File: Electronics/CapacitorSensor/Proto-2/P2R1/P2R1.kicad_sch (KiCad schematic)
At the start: 48 parts

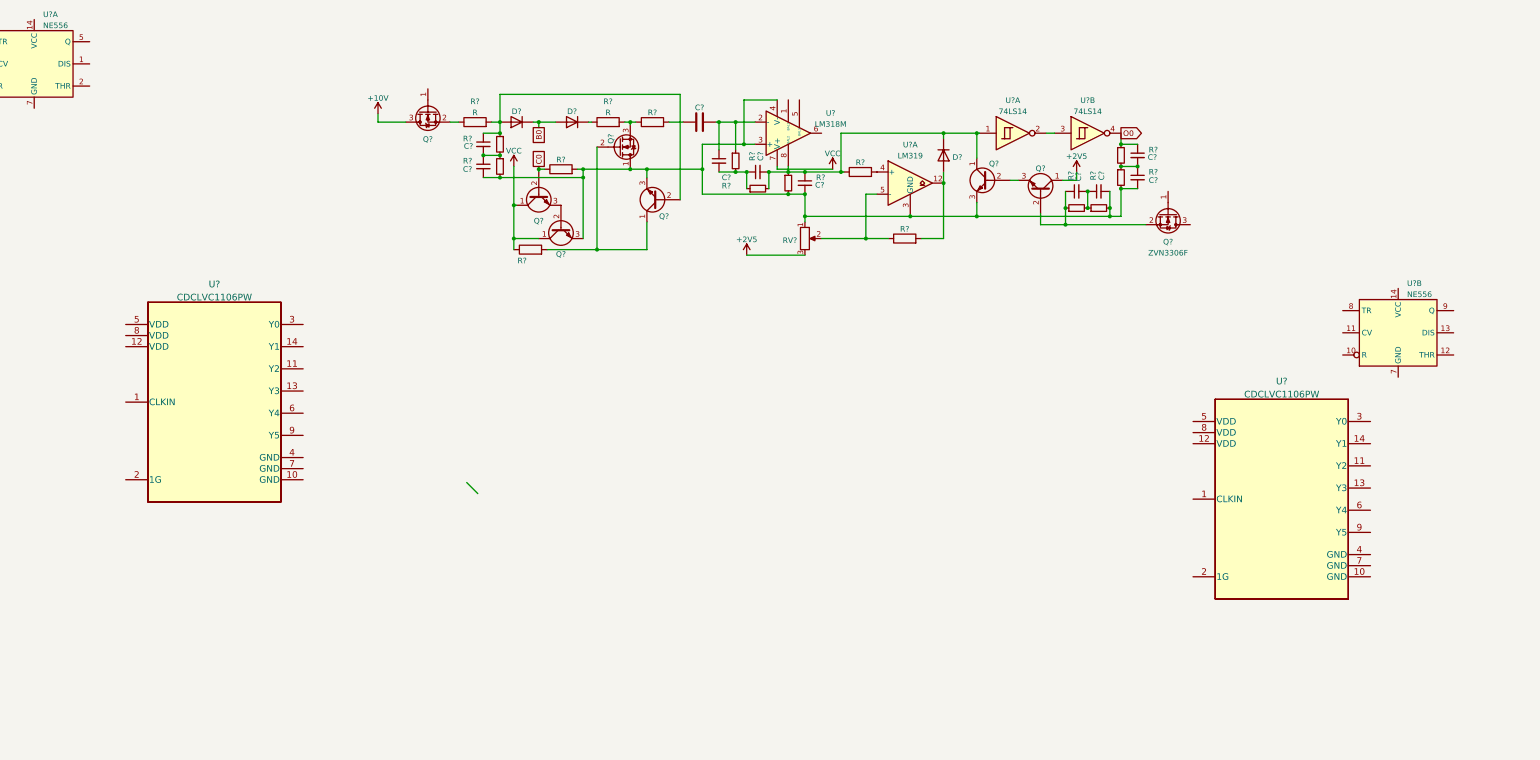
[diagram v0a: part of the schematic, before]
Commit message: Decided to continue work on other laptop. Added forgotten resistor to P2R1
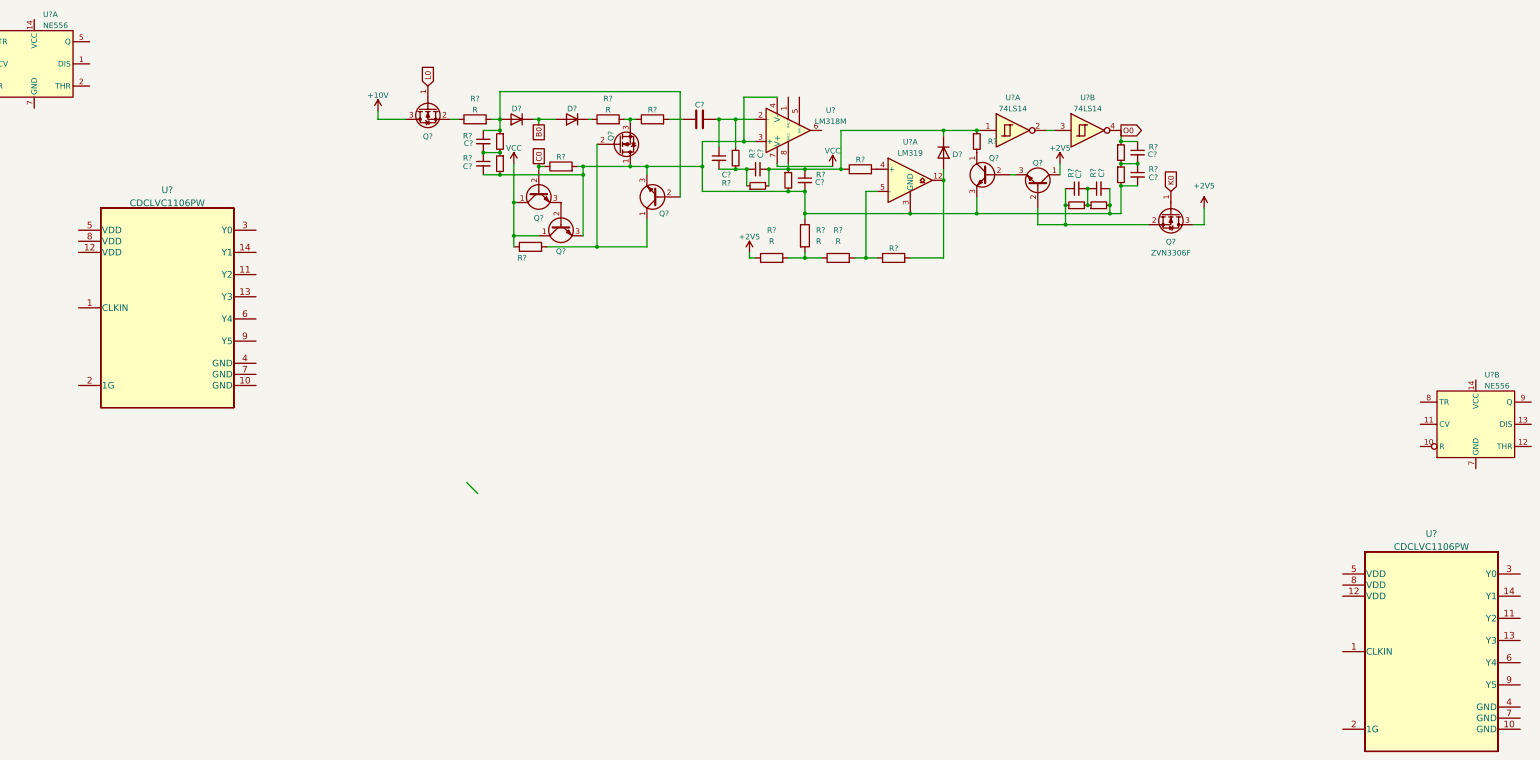
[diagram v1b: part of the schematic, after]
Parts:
- removed RV?: R_Potentiometer, Potentiometer_SMD:Potentiometer_Bourns_3214G_Horizontal, symbol Device:R_Potentiometer
- added R? (x3): R, symbol Device:R
- added R?: R_Small, symbol Device:R_Small
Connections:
- net +2V5: now also Q?.3 (D), R?.1
- net at C?.2, C?.2, C?.2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: now also R?.1
- net at C?.1, C?.2, D?.1 (K)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: now also R?.1; no longer Q?.1 (C)
- net L0: now reaches Q?.1 (G)
- net K0: now reaches Q?.1 (G)
- net at R?.1, U?.5 (-): now also R?.2
- new net: R?.1, R?.2, R?.2
- new net: Q?.1 (C), R?.2
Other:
- moved on the sheet: C?, D?, Q?, R?, U?, U?A, U?B

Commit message: Updated stuff
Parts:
- added R? (x2): R, symbol Device:R
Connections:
- net at C?.2, C?.2, C?.2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: now also R?.2
- net at C?.1, C?.2, D?.1 (K)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: now also R?.1; no longer R?.1, U?.1
- net at D?.2 (A), Q?.2 (B), R?.2: no longer C?.1, R?.1
- new net: C?.1, R?.1, R?.1, R?.1, R?.2, U?.1
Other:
- moved on the sheet: C?, Q?, R?, U?A, U?B

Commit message: a lot of work went into this
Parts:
- removed Q?: ZVN3306F, Package_TO_SOT_SMD:SOT-23, symbol Transistor_FET:ZVN3306F
- added C?: C_Polarized, symbol Device:C_Polarized
- added R? (x3): R_Small, symbol Device:R_Small
- added R? (x2): R, symbol Device:R
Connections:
- net GNDA: now reaches C?.2, C?.2, C?.2, C?.2, Q?.1 (D), Q?.3 (E), Q?.3 (E), Q?.3 (E), R?.1, R?.2, R?.2, R?.2, R?.2, R?.2, R?.2, U?.3 (+), U?.3 (GND), U?.4 (V-)
- net GNDA: now also R?.1
- net at C?.1, Q?.2 (B), R?.1: now also R?.1, R?.2
- net +5V: now reaches U?.10 (R)
- net +5V: now also U?.14 (VCC), R?.1, R?.2
- net at U?.12 (THR): now also U?.8 (TR), C?.1, R?.2
- net at U?.13 (DIS): now also R?.1, R?.2
- net GND: now reaches U?.7 (GND)
- net GND: now also C?.2
- net at U?.9 (Q): now also R?.1, R?.2
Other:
- moved on the sheet: U?B
